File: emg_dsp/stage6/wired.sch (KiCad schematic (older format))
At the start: 53 parts, among them U38 OMNETICS_36, U41 MIC5365-2.5, U42 TC1016-3.0, U43 TC1016-3.0, U44 AD7980, U45 AD7980, U46 ADR381, U47 8X100, U48 8X100, U49 TC1016-3.0, U50 IL715-3, U51 DCP01DB, U52 IL715-3, U92 RHA2116, U93 RHA2116

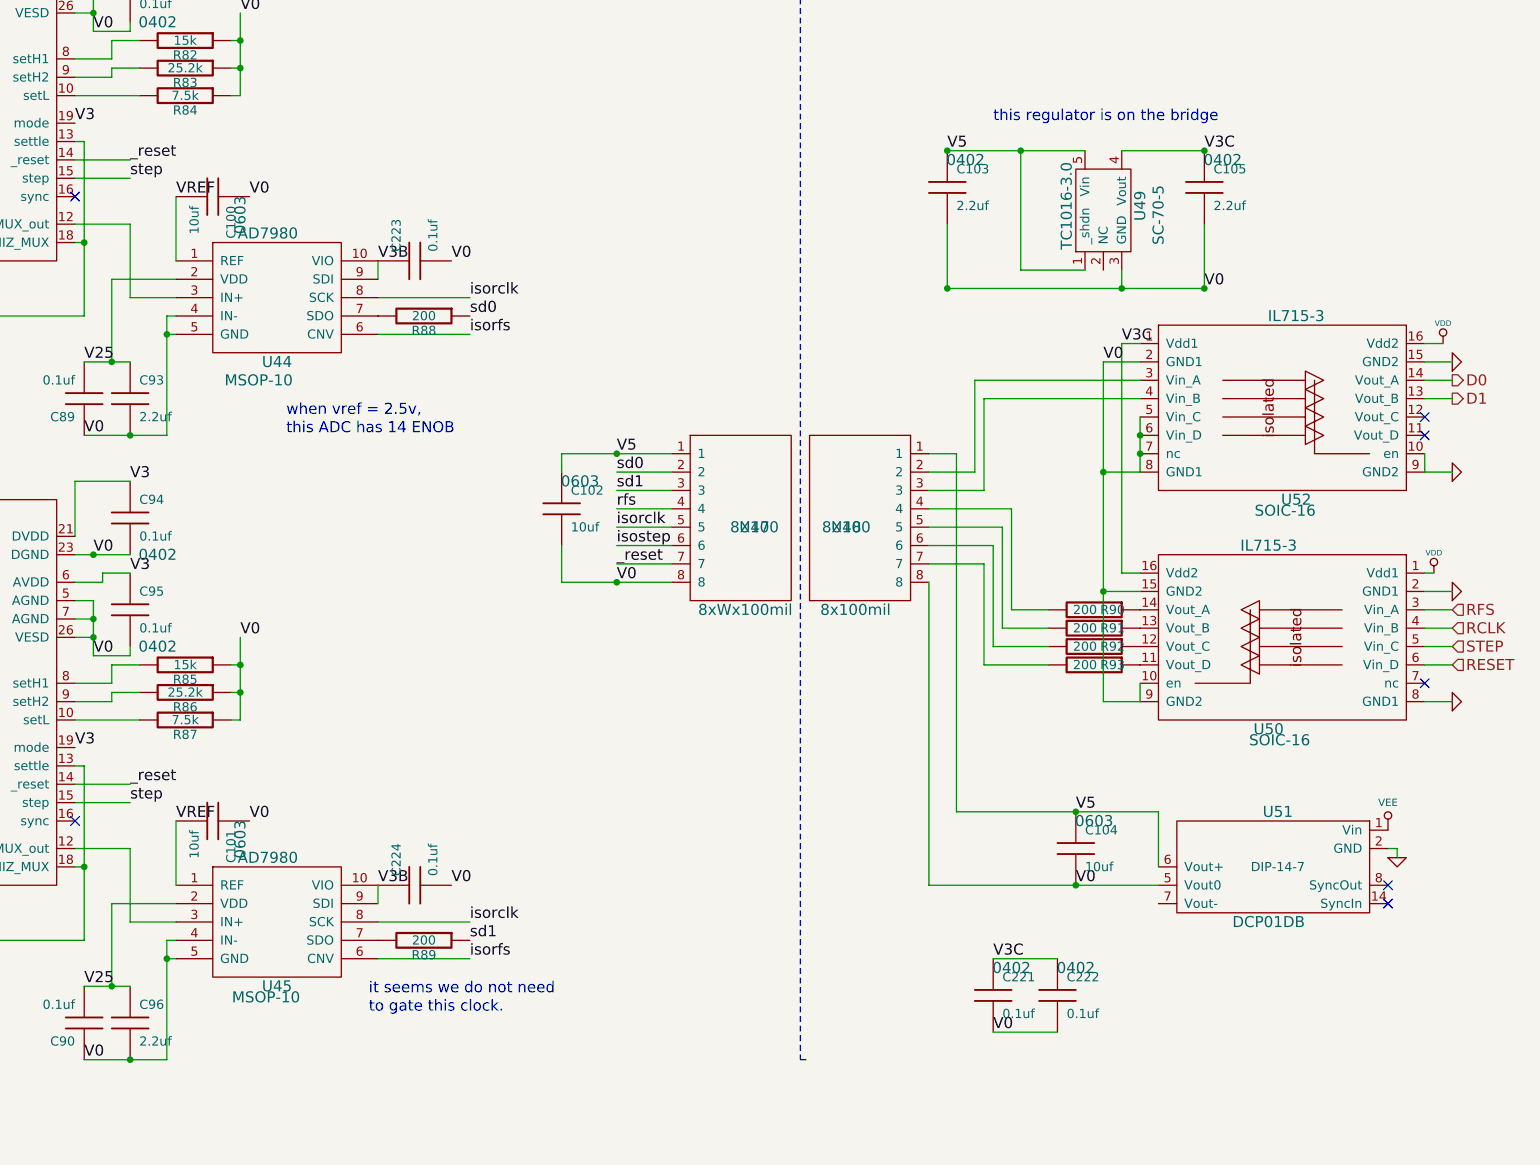
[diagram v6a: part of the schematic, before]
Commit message: getting the last of the nets (GND, Vdd, Vcc) routed. still need to check the pinouts, etc.
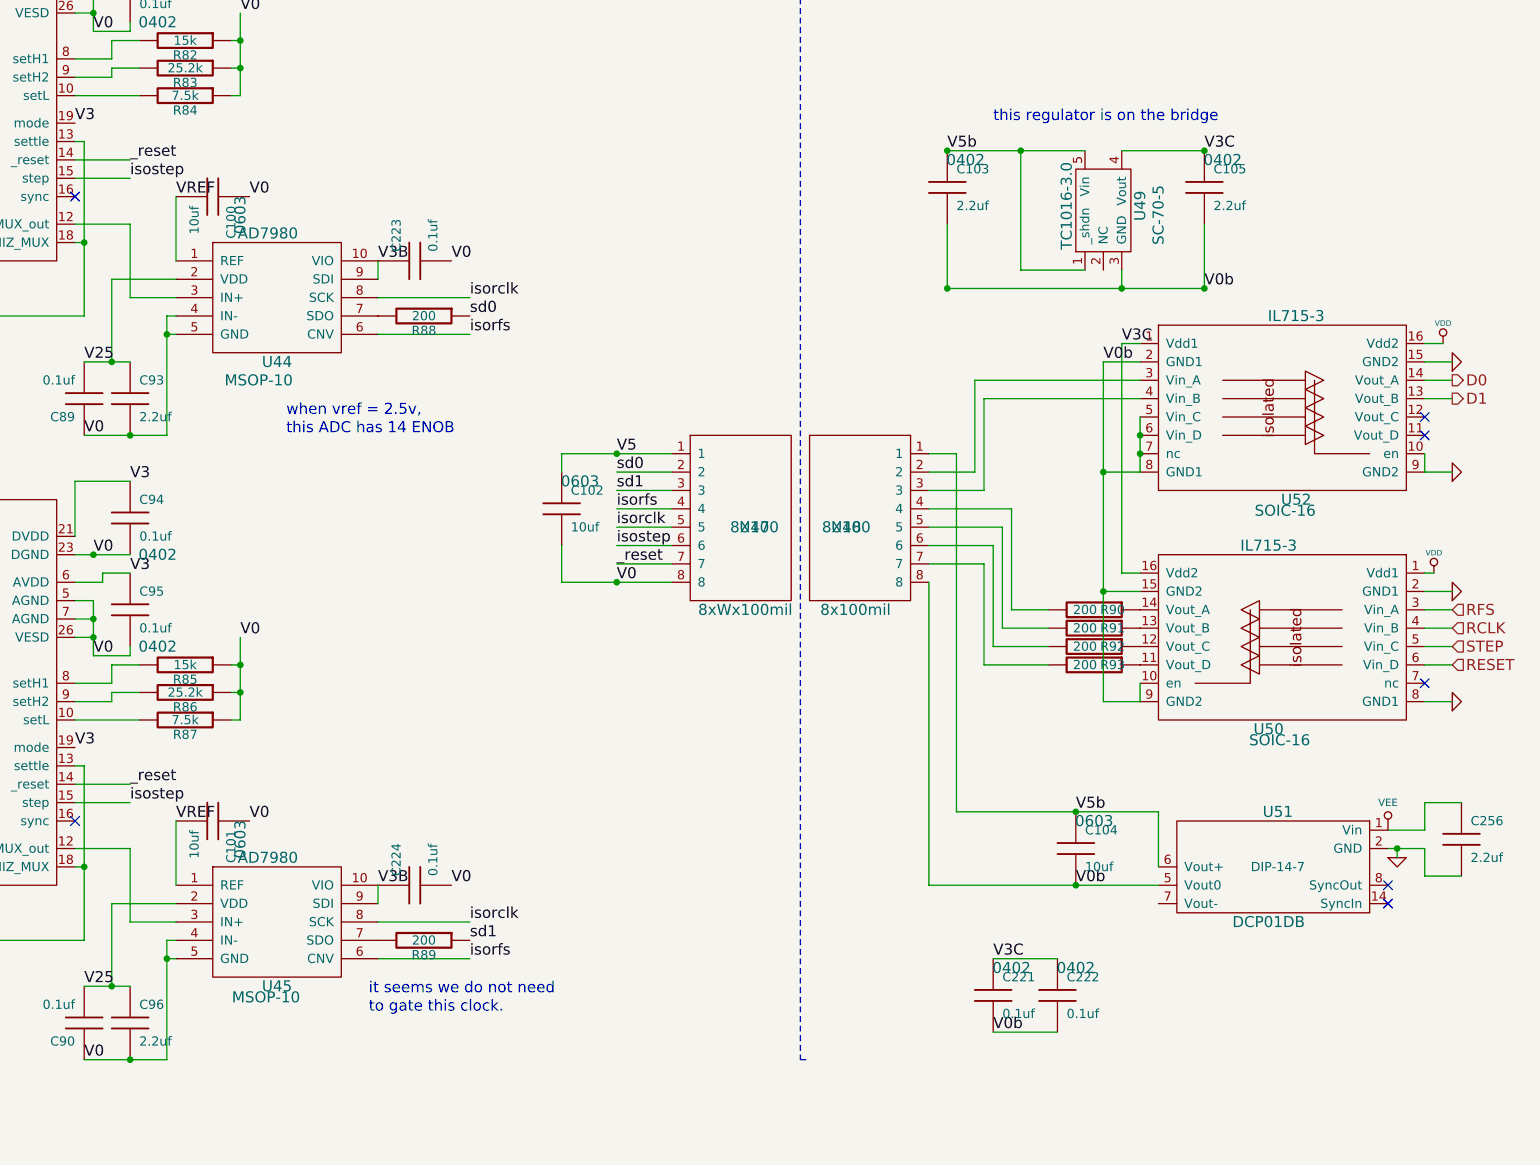
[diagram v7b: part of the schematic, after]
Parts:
- added C256: 2.2uf, 0402, symbol C
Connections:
- net rfs is gone; now on net isorfs: U47.4
- net step is gone; now on net isostep: U92.15 (step), U93.15 (step)
- net GND: now also C256.2
- net V0: no longer C103.2, C104.2, C105.2, C221.2, C222.2, U48.8, U49.3 (GND), U50.10 (en), U50.15 (GND2), U50.9 (GND2), U51.5 (Vout0), U52.2 (GND1), U52.5 (Vin_C), U52.6 (Vin_D), U52.7 (nc), U52.8 (GND1)
- net V5: no longer C103.1, C104.1, U48.1, U49.1 (_shdn), U49.5 (Vin), U51.6 (Vout+)
- net VEE: now also C256.1
- new net V0b: C103.2, C104.2, C105.2, C221.2, C222.2, U48.8, U49.3 (GND), U50.10 (en), U50.15 (GND2), U50.9 (GND2), U51.5 (Vout0), U52.2 (GND1), U52.5 (Vin_C), U52.6 (Vin_D), U52.7 (nc), U52.8 (GND1)
- new net V5b: C103.1, C104.1, U48.1, U49.1 (_shdn), U49.5 (Vin), U51.6 (Vout+)
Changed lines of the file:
@@
-EESchema Schematic File Version 2  date Thu 30 Sep 2010 11:24:56 PM EDT
+EESchema Schematic File Version 2  date Tue 05 Oct 2010 01:02:39 AM EDT
 LIBS:power
 LIBS:device
@@
 Sheet 13 15
 Title "Stage 4 / Copyright 2010 Timothy L Hanson "
-Date "1 oct 2010"
+Date "5 oct 2010"
 Rev ""
 Comp "This design is free: redistribute or modify under the GPL v. 3 or later"
@@
 Comment4 ""
 $EndDescr
+Connection ~ 12050 6200
+Wire Wire Line
+	12400 6350 12200 6350
+Wire Wire Line
+	12200 6200 12200 6350
+Wire Wire Line
+	12000 6200 12200 6200
 Wire Wire Line
 	9500 4750 9500 6400
@@
 	9900 4450 9500 4450
 Wire Wire Line
-	12050 6250 12050 6200
-Wire Wire Line
-	12050 6200 12000 6200
+	12050 6200 12050 6250
 Wire Wire Line
 	10150 5100 9850 5100
@@
 Wire Wire Line
 	9650 6000 10750 6000
+Wire Wire Line
+	12000 6100 12200 6100
+Wire Wire Line
+	12200 6100 12200 5950
+Wire Wire Line
+	12200 5950 12400 5950
+$Comp
+L C C256
+U 1 1 4CAAB0E7
+P 12400 6150
+F 0 "C256" H 12450 6250 50  0000 L CNN
+F 1 "2.2uf" H 12450 6050 50  0000 L CNN
+F 2 "0402" H 12500 6300 60  0001 C CNN
+	1    12400 6150
+	1    0    0    -1
+$EndComp
 Text Label 6900 6400 0    60   ~ 0
 V0
@@
 V3C
 Text Label 9850 7200 0    60   ~ 0
-V0
+V0b
 $Comp
 L C C222
@@
 when vref = 2.5v,
 Text Label 10300 6400 0    60   ~ 0
-V0
+V0b
 Text Label 10300 6000 0    60   ~ 0
-V5
+V5b
 Text Notes 6450 7100 0    60   ~ 0
 to gate this clock.
@@
 NoConn ~ 12200 3850
 $Comp
-L GND #PWR0302
+L GND #PWR201
 U 1 1 4C9B921B
 P 12350 4800
-F 0 "#PWR0302" H 12350 4800 30  0001 C CNN
+F 0 "#PWR201" H 12350 4800 30  0001 C CNN
 F 1 "GND" H 12350 4730 30  0001 C CNN
 	1    12350 4800
@@
 $EndComp
 $Comp
-L VDD #PWR0303
+L VDD #PWR197
 U 1 1 4C9B9218
 P 12250 4700
-F 0 "#PWR0303" H 12250 4800 30  0001 C CNN
+F 0 "#PWR197" H 12250 4800 30  0001 C CNN
 F 1 "VDD" H 12250 4810 30  0000 C CNN
 	1    12250 4700
@@
 $EndComp
 $Comp
-L GND #PWR0304
+L GND #PWR202
 U 1 1 4C9B9215
 P 12350 5400
-F 0 "#PWR0304" H 12350 5400 30  0001 C CNN
+F 0 "#PWR202" H 12350 5400 30  0001 C CNN
 F 1 "GND" H 12350 5330 30  0001 C CNN
 	1    12350 5400
@@
 $EndComp
 $Comp
-L GND #PWR0305
+L GND #PWR200
 U 1 1 4C9B9212
 P 12350 4150
-F 0 "#PWR0305" H 12350 4150 30  0001 C CNN
+F 0 "#PWR200" H 12350 4150 30  0001 C CNN
 F 1 "GND" H 12350 4080 30  0001 C CNN
 	1    12350 4150
@@
 $EndComp
 $Comp
-L GND #PWR0306
+L GND #PWR199
 U 1 1 4C9B920A
 P 12350 3550
-F 0 "#PWR0306" H 12350 3550 30  0001 C CNN
+F 0 "#PWR199" H 12350 3550 30  0001 C CNN
 F 1 "GND" H 12350 3480 30  0001 C CNN
 	1    12350 3550
@@
 $EndComp
 $Comp
-L VDD #PWR0307
+L VDD #PWR198
 U 1 1 4C9B9204
 P 12300 3450
-F 0 "#PWR0307" H 12300 3550 30  0001 C CNN
+F 0 "#PWR198" H 12300 3550 30  0001 C CNN
 F 1 "VDD" H 12300 3560 30  0000 C CNN
 	1    12300 3450
@@
 this regulator is on the bridge
 Text Label 11000 3150 0    60   ~ 0
-V0
+V0b
 Text Label 9600 2400 0    60   ~ 0
-V5
+V5b
 $Comp
 L C C105
@@
 $EndComp
 Text Label 10450 3550 0    60   ~ 0
-V0
+V0b
 Text Label 7000 6600 0    60   ~ 0
 isorclk
@@
 isorclk
 Text Label 7800 4350 0    60   ~ 0
-rfs
+isorfs
 $Comp
 L C C90
@@
 _reset
 Text Label 5150 5950 0    60   ~ 0
-step
+isostep
 $Comp
 L R R89
@@
 $EndComp
 $Comp
-L GND #PWR0308
+L GND #PWR196
 U 1 1 4C9B8790
 P 12050 6250
-F 0 "#PWR0308" H 12050 6250 30  0001 C CNN
+F 0 "#PWR196" H 12050 6250 30  0001 C CNN
 F 1 "GND" H 12050 6180 30  0001 C CNN
 	1    12050 6250
@@
 $EndComp
 $Comp
-L VEE #PWR193
+L VEE #PWR195
 U 1 1 4C9B878C
 P 12000 6100
-F 0 "#PWR193" H 12000 6300 40  0001 C CNN
+F 0 "#PWR195" H 12000 6300 40  0001 C CNN
 F 1 "VEE" H 12000 6250 40  0000 C CNN
 	1    12000 6100
@@
 $EndComp
 Text Label 5150 2550 0    60   ~ 0
-step
+isostep
 Text Label 5150 2450 0    60   ~ 0
 _reset
@@
 $EndComp
 $Comp
-L GND #PWR0309
+L GND #PWR194
 U 1 1 4CA0ED85
 P 4100 10400
-F 0 "#PWR0309" H 4100 10400 30  0001 C CNN
+F 0 "#PWR194" H 4100 10400 30  0001 C CNN
 F 1 "GND" H 4100 10330 30  0001 C CNN
 	1    4100 10400

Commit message: board getting done! next up is silkscreen - pita.
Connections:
- net GND: no longer U41.2 (GND)
- net V0: now also U41.2 (GND)
